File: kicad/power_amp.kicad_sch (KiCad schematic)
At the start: 15 parts

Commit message: Datasheet footprints, floor-plan placement, headless autoroute (144/145, DRC 0)
PCB-AUDIT s1 fixes with datasheet-derived project footprints:
- TO-220-5_Vertical_P1.70mm_LM1875 (TI NDH0005D): 1.45 mm pads on the 1.1 mm
  drill -> 0.175 mm annular (was 0.0875, 5 DRC errors); pad-local 0.2 mm clearance
- Bridge_KBP_P3.81mm (Diodes DS39310 KBP404G-KBP410G, pins + ~ ~ -); bridge
  symbol renumbered to the physical order; errata #3 updated (KBU needs a swap)
- value-aware CP/R sizing (real can sizes for 4700/2200/1000 uF, 5 W / 1 W
  resistors, fat pads on the 0R speaker return); Part 4 wire pads for all
  off-board wiring (2.0 mm/1.2 mm signal, 3.0 mm/1.5 mm speaker + transformer)
- VRAW/AC1/AC2 moved into the HighCurrent net class (errata #11)

gen_pcb.py now places to the Part 5 floor plan: balanced columns (Input/Preamp
with Tone stacked below | Reverb/Trem/MRB | Power Amp | PSU), signal order inside
zones with serpentine shelves, LM1875/LM317 on the top edge with the 10 mm
keep-out, wiring edge along the bottom, 4x M3 holes, two locked 0.9 mm escape
stubs off the LM1875 pins 4/5 (a 1.5/2.5 mm trace cannot enter a 1.70 mm pitch).
DRC before routing: 0 errors, 0 warnings.

route_board.py: pcbnew DSN export -> Freerouting -> SES import -> pour refill.
Freerouting 2.1.0 ignores every pass/timeout limit in CLI mode and only writes
output at 0 unrouted (and its MT router crashed), so the script drives 1.9.0
under xvfb-run and injects autoroute_settings (bottom layer 6x cost, via 80) so
the GND pour stays whole. Committed board: 144/145 connections routed, 0 DRC
violations (--severity-all), 26 vias, 351 mm on the bottom vs 3.7 m on top; the
one open PA_OUT link (blocked by R_bias1) is documented as a GUI finish.

Chassis-fit figure corrected: the old 48-53 % / 82-90 % densities counted hidden
text boxes; text-less it is ~33 % on 190x115 and ~56 % on 155x90.

Docs: PCB-NOTES/PCB-AUDIT rewritten, README, CHANGELOG, errata #3/#11,
SOURCES (package drawings), Part 10, kicad RE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
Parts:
- C_byp2, C_gain: footprint Capacitor_THT:CP_Radial_D8.0mm_P3.50mm -> Capacitor_THT:CP_Radial_D5.0mm_P2.00mm
- C_out: footprint Capacitor_THT:CP_Radial_D8.0mm_P3.50mm -> Capacitor_THT:CP_Radial_D16.0mm_P7.50mm
- IC_PA: footprint Package_TO_SOT_THT:TO-220-5_Vertical -> cambridge_reverb:TO-220-5_Vertical_P1.70mm_LM1875
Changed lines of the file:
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@@
     (pin "1")
     (pin "2")
-    (instances (project "cambridge_reverb" (path "/43bb109b-155d-4d3a-b8db-475f98dada40" (reference "C_in_pa") (unit 1))))
+    (instances (project "cambridge_reverb" (path "/97e5b5ba-e7d2-4f7c-be8d-4c4f23c84681" (reference "C_in_pa") (unit 1))))
   )
   (wire (pts (xy 129.54 120.64999999999999) (xy 127.0 120.64999999999999)) (stroke (width 0) (type default)))
@@
     (pin "1")
     (pin "2")
-    (instances (project "cambridge_reverb" (path "/43bb109b-155d-4d3a-b8db-475f98dada40" (reference "R_bias1") (unit 1))))
+    (instances (project "cambridge_reverb" (path "/97e5b5ba-e7d2-4f7c-be8d-4c4f23c84681" (reference "R_bias1") (unit 1))))
   )
   (wire (pts (xy 129.54 95.25) (xy 127.0 95.25)) (stroke (width 0) (type default)))
@@
     (pin "1")
     (pin "2")
-    (instances (project "cambridge_reverb" (path "/43bb109b-155d-4d3a-b8db-475f98dada40" (reference "R_bias2") (unit 1))))
+    (instances (project "cambridge_reverb" (path "/97e5b5ba-e7d2-4f7c-be8d-4c4f23c84681" (reference "R_bias2") (unit 1))))
   )
   (wire (pts (xy 129.54 146.05) (xy 127.0 146.05)) (stroke (width 0) (type default)))
@@
     (property "Reference" "IC_PA" (at 208.28 123.19 0) (effects (font (size 1.27 1.27)) (justify left)))
     (property "Value" "LM1875T" (at 208.28 125.73 0) (effects (font (size 1.27 1.27)) (justify left)))
-    (property "Footprint" "Package_TO_SOT_THT:TO-220-5_Vertical" (at 205.74 130.81 0) (effects (font (size 1.27 1.27)) hide))
+    (property "Footprint" "cambridge_reverb:TO-220-5_Vertical_P1.70mm_LM1875" (at 205.74 130.81 0) (effects (font (size 1.27 1.27)) hide))
     (pin "1")
     (pin "2")
@@
     (pin "5")
     (pin "3")
-    (instances (project "cambridge_reverb" (path "/43bb109b-155d-4d3a-b8db-475f98dada40" (reference "IC_PA") (unit 1))))
+    (instances (project "cambridge_reverb" (path "/97e5b5ba-e7d2-4f7c-be8d-4c4f23c84681" (reference "IC_PA") (unit 1))))
   )
   (wire (pts (xy 193.04 128.26999999999998) (xy 190.5 128.26999999999998)) (stroke (width 0) (type default)))
@@
     (pin "1")
     (pin "2")
-    (instances (project "cambridge_reverb" (path "/43bb109b-155d-4d3a-b8db-475f98dada40" (reference "R_fb") (unit 1))))
+    (instances (project "cambridge_reverb" (path "/97e5b5ba-e7d2-4f7c-be8d-4c4f23c84681" (reference "R_fb") (unit 1))))
   )
   (wire (pts (xy 240.03 100.33) (xy 237.49 100.33)) (stroke (width 0) (type default)))
@@
     (pin "1")
     (pin "2")
-    (instances (project "cambridge_reverb" (path "/43bb109b-155d-4d3a-b8db-475f98dada40" (reference "C_fb_hf") (unit 1))))
+    (instances (project "cambridge_reverb" (path "/97e5b5ba-e7d2-4f7c-be8d-4c4f23c84681" (reference "C_fb_hf") (unit 1))))
   )
   (wire (pts (xy 240.03 81.28) (xy 237.49 81.28)) (stroke (width 0) (type default)))
@@
     (pin "1")
     (pin "2")
-    (instances (project "cambridge_reverb" (path "/43bb109b-155d-4d3a-b8db-475f98dada40" (reference "R_gain") (unit 1))))
+    (instances (project "cambridge_reverb" (path "/97e5b5ba-e7d2-4f7c-be8d-4c4f23c84681" (reference "R_gain") (unit 1))))
   )
   (wire (pts (xy 160.01999999999998 170.18) (xy 157.48 170.18)) (stroke (width 0) (type default)))
@@
     (property "Reference" "C_gain" (at 208.28 162.56 0) (effects (font (size 1.27 1.27)) (justify left)))
     (property "Value" "22uF/25V" (at 208.28 165.1 0) (effects (font (size 1.27 1.27)) (justify left)))
-    (property "Footprint" "Capacitor_THT:CP_Radial_D8.0mm_P3.50mm" (at 205.74 170.18 0) (effects (font (size 1.27 1.27)) hide))
+    (property "Footprint" "Capacitor_THT:CP_Radial_D5.0mm_P2.00mm" (at 205.74 170.18 0) (effects (font (size 1.27 1.27)) hide))
     (pin "1")
     (pin "2")
-    (instances (project "cambridge_reverb" (path "/43bb109b-155d-4d3a-b8db-475f98dada40" (reference "C_gain") (unit 1))))
+    (instances (project "cambridge_reverb" (path "/97e5b5ba-e7d2-4f7c-be8d-4c4f23c84681" (reference "C_gain") (unit 1))))
   )
   (wire (pts (xy 200.66 170.18) (xy 198.12 170.18)) (stroke (width 0) (type default)))
@@
     (pin "1")
     (pin "2")
-    (instances (project "cambridge_reverb" (path "/43bb109b-155d-4d3a-b8db-475f98dada40" (reference "R_zobel") (unit 1))))
+    (instances (project "cambridge_reverb" (path "/97e5b5ba-e7d2-4f7c-be8d-4c4f23c84681" (reference "R_zobel") (unit 1))))
   )
   (wire (pts (xy 250.19 161.29) (xy 247.65 161.29)) (stroke (width 0) (type default)))
@@
     (pin "1")
     (pin "2")
-    (instances (project "cambridge_reverb" (path "/43bb109b-155d-4d3a-b8db-475f98dada40" (reference "C_zobel") (unit 1))))
+    (instances (project "cambridge_reverb" (path "/97e5b5ba-e7d2-4f7c-be8d-4c4f23c84681" (reference "C_zobel") (unit 1))))
   )
   (wire (pts (xy 280.66999999999996 161.29) (xy 278.13 161.29)) (stroke (width 0) (type default)))
@@
     (property "Reference" "C_out" (at 257.81 123.19 0) (effects (font (size 1.27 1.27)) (justify left)))
     (property "Value" "2200uF/35V" (at 257.81 125.73 0) (effects (font (size 1.27 1.27)) (justify left)))
-    (property "Footprint" "Capacitor_THT:CP_Radial_D8.0mm_P3.50mm" (at 255.27 130.81 0) (effects (font (size 1.27 1.27)) hide))
+    (property "Footprint" "Capacitor_THT:CP_Radial_D16.0mm_P7.50mm" (at 255.27 130.81 0) (effects (font (size 1.27 1.27)) hide))
     (pin "1")
     (pin "2")
-    (instances (project "cambridge_reverb" (path "/43bb109b-155d-4d3a-b8db-475f98dada40" (reference "C_out") (unit 1))))
+    (instances (project "cambridge_reverb" (path "/97e5b5ba-e7d2-4f7c-be8d-4c4f23c84681" (reference "C_out") (unit 1))))
   )
   (wire (pts (xy 250.19 130.81) (xy 247.65 130.81)) (stroke (width 0) (type default)))
@@
     (pin "1")
     (pin "2")
-    (instances (project "cambridge_reverb" (path "/43bb109b-155d-4d3a-b8db-475f98dada40" (reference "D1") (unit 1))))
+    (instances (project "cambridge_reverb" (path "/97e5b5ba-e7d2-4f7c-be8d-4c4f23c84681" (reference "D1") (unit 1))))
   )
   (wire (pts (xy 240.03 200.66000000000003) (xy 237.49 200.66000000000003)) (stroke (width 0) (type default)))
@@
     (pin "1")
     (pin "2")
-    (instances (project "cambridge_reverb" (path "/43bb109b-155d-4d3a-b8db-475f98dada40" (reference "D2") (unit 1))))
+    (instances (project "cambridge_reverb" (path "/97e5b5ba-e7d2-4f7c-be8d-4c4f23c84681" (reference "D2") (unit 1))))
   )
   (wire (pts (xy 280.66999999999996 200.66000000000003) (xy 278.13 200.66000000000003)) (stroke (width 0) (type default)))
@@
     (pin "1")
     (pin "2")
-    (instances (project "cambridge_reverb" (path "/43bb109b-155d-4d3a-b8db-475f98dada40" (reference "C_byp1") (unit 1))))
+    (instances (project "cambridge_reverb" (path "/97e5b5ba-e7d2-4f7c-be8d-4c4f23c84681" (reference "C_byp1") (unit 1))))
   )
   (wire (pts (xy 129.54 200.66000000000003) (xy 127.0 200.66000000000003)) (stroke (width 0) (type default)))
@@
     (property "Reference" "C_byp2" (at 172.72 193.04000000000002 0) (effects (font (size 1.27 1.27)) (justify left)))
     (property "Value" "10uF/50V" (at 172.72 195.58 0) (effects (font (size 1.27 1.27)) (justify left)))
-    (property "Footprint" "Capacitor_THT:CP_Radial_D8.0mm_P3.50mm" (at 170.18 200.66000000000003 0) (effects (font (size 1.27 1.27)) hide))
+    (property "Footprint" "Capacitor_THT:CP_Radial_D5.0mm_P2.00mm" (at 170.18 200.66000000000003 0) (effects (font (size 1.27 1.27)) hide))
     (pin "1")
     (pin "2")
-    (instances (project "cambridge_reverb" (path "/43bb109b-155d-4d3a-b8db-475f98dada40" (reference "C_byp2") (unit 1))))
+    (instances (project "cambridge_reverb" (path "/97e5b5ba-e7d2-4f7c-be8d-4c4f23c84681" (reference "C_byp2") (unit 1))))
   )
   (wire (pts (xy 165.10000000000002 200.66000000000003) (xy 162.56 200.66000000000003)) (stroke (width 0) (type default)))

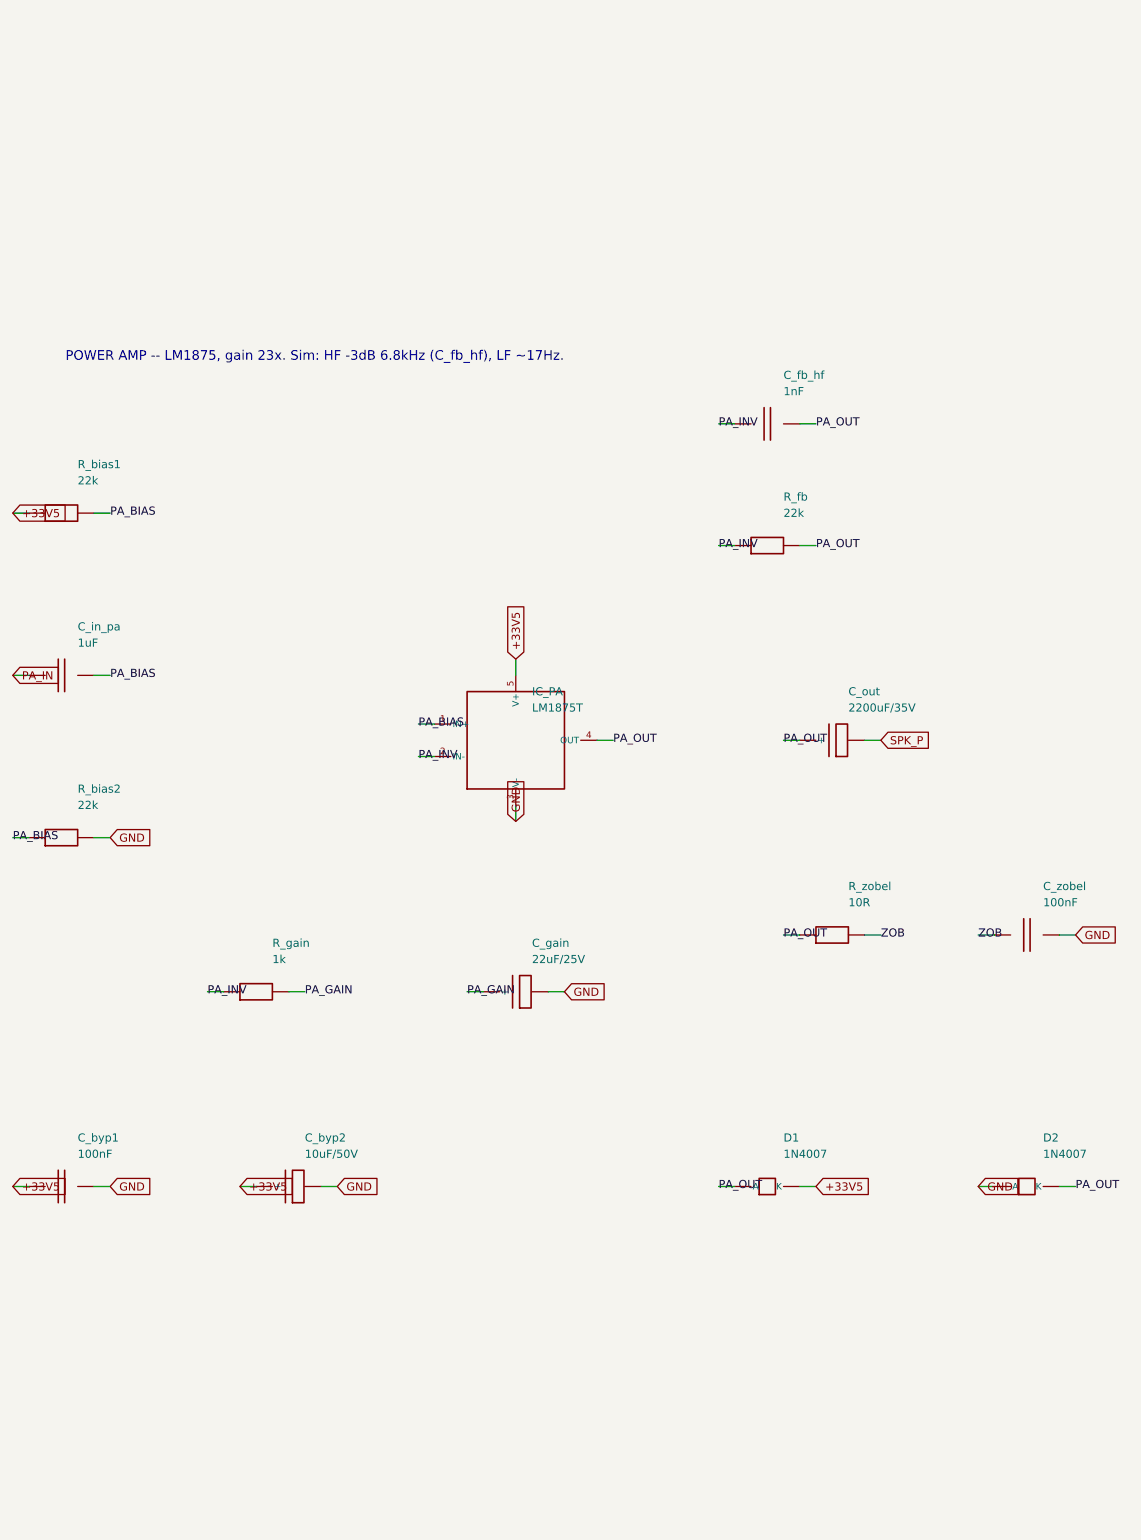
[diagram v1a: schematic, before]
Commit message: Add 26 labelled bench test points (schematic + BOM + silk) and re-route
Test points follow the Part 5 bring-up order: rails (VRAW, +33V5, VREG_IN,
+17V), JFET drains Q1D/Q2D/QRD (the errata #15 bias trim), the VBIAS_R/VBIAS_T
mid-rail refs, every inter-stage node (PREAMP_OUT, TONE_OUT, BLEND, TREM_OUT,
MRB_OUT, PA_IN), tank drive/return, LFO, PA_BIAS/PA_OUT/SPK_P, and a GND pin
per zone for the probe clip.

- gen_kicad.py: one-pin TP symbol; TEST_POINTS table; add_test_points() puts
  them on their sheets so they are in the netlist and the BOM (one order line)
- footprint TestPoint_THT_D2.0mm_Label: 2.0 mm pad / 1.0 mm drill for a header
  pin or wire loop; the footprint VALUE (= net alias) prints on F.SilkS
- gen_pcb.py: test-point strip across the top of each zone; the effects column
  is now two stacked zones (tremolo+MRB above, reverb below next to its tank
  pads) so each block's points sit right above its parts; stacked-zone gap 2 mm
- PCB-NOTES.md: test-point table with expected values (Part 3 troubleshooting,
  Part 2 set-up, ngspice) and the bring-up sequence
- Re-routed (Freerouting 1.9.0, B.Cu x7, via 60): 161/166 connections, 0 DRC
  violations, 54 vias; the five open links are listed for a GUI finish

Co-Authored-By: Claude Fable 5.1 <noreply@anthropic.com>
Claude-Session: https://claude.ai/code/session_01Vk8HkvCugxFpQsBPVnNT2H
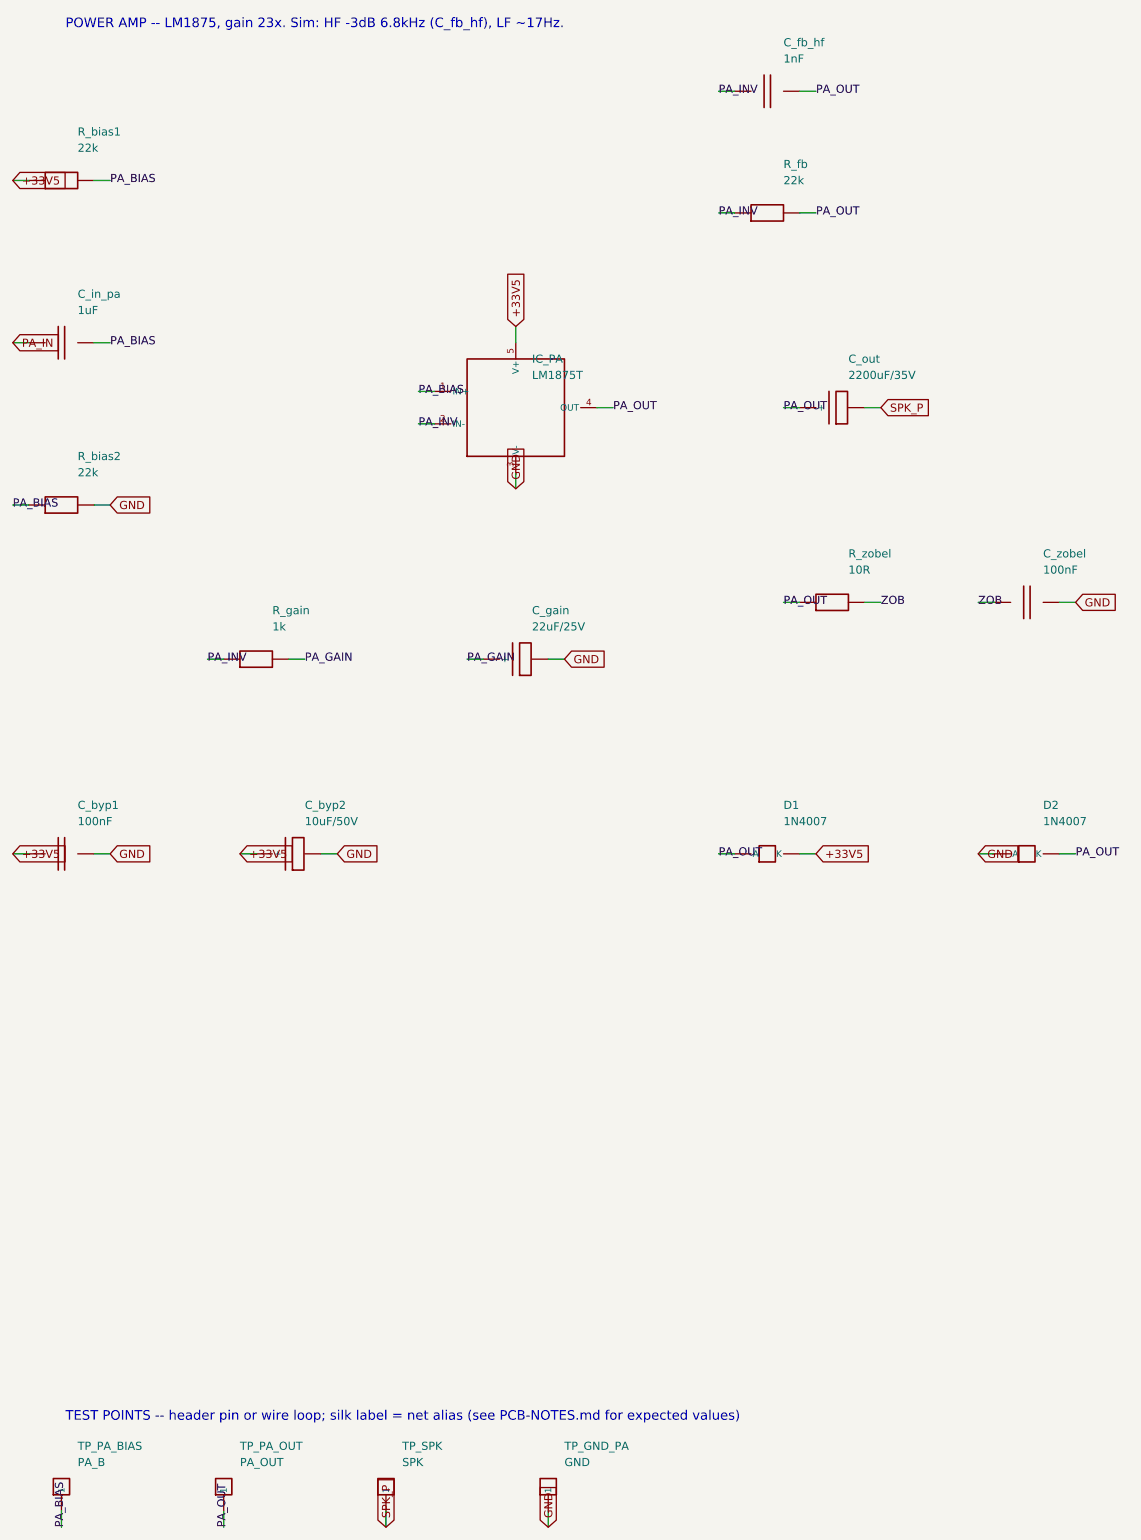
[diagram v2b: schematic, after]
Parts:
- added TP_GND_PA: GND, cambridge_reverb:TestPoint_THT_D2.0mm_Label, symbol cr_primitives:TP
- added TP_PA_BIAS: PA_B, cambridge_reverb:TestPoint_THT_D2.0mm_Label, symbol cr_primitives:TP
- added TP_PA_OUT: PA_OUT, cambridge_reverb:TestPoint_THT_D2.0mm_Label, symbol cr_primitives:TP
- added TP_SPK: SPK, cambridge_reverb:TestPoint_THT_D2.0mm_Label, symbol cr_primitives:TP
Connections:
- net GND: now also TP_GND_PA.1
- net PA_BIAS: now also TP_PA_BIAS.1
- net PA_OUT: now also TP_PA_OUT.1
- net SPK_P: now also TP_SPK.1
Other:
- note added: "TEST POINTS -- header pin or wire loop; silk label = net alias (see PCB-NOTES.md for expected values)"
